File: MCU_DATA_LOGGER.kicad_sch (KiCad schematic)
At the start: 0 parts

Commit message: Have added symbols
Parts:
- added BT?: Battery, symbol Device:Battery
- added C? (x4): C, symbol Device:C
- added C?: C_Polarized, symbol Device:C_Polarized
- added D? (x3): LED, symbol Device:LED
- added H? (x4): MountingHole, symbol Mechanical:MountingHole
- added R? (x7): R, symbol Device:R
- added U? (x2): 24LC1025, symbol Memory_EEPROM:24LC1025
- added U?: ATMEGA328P-AU, QFP80P900X900X120-32N, symbol ATMEGA328P-AU:ATMEGA328P-AU
- added U?: DS1337S+, SOIC127P600X175-8N, symbol New_Library:DS1337S+
- added Y? (x2): Crystal, symbol Device:Crystal
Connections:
- new net: D?.1 (K), D?.1 (K)
- new net: D?.2 (A), D?.2 (A)
- new net: U?.21 (GND), U?.3 (GND), U?.5 (GND)
- new net: U?.4 (VCC), U?.6 (VCC)
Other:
- added sheet Connectors (connectors.kicad_sch)

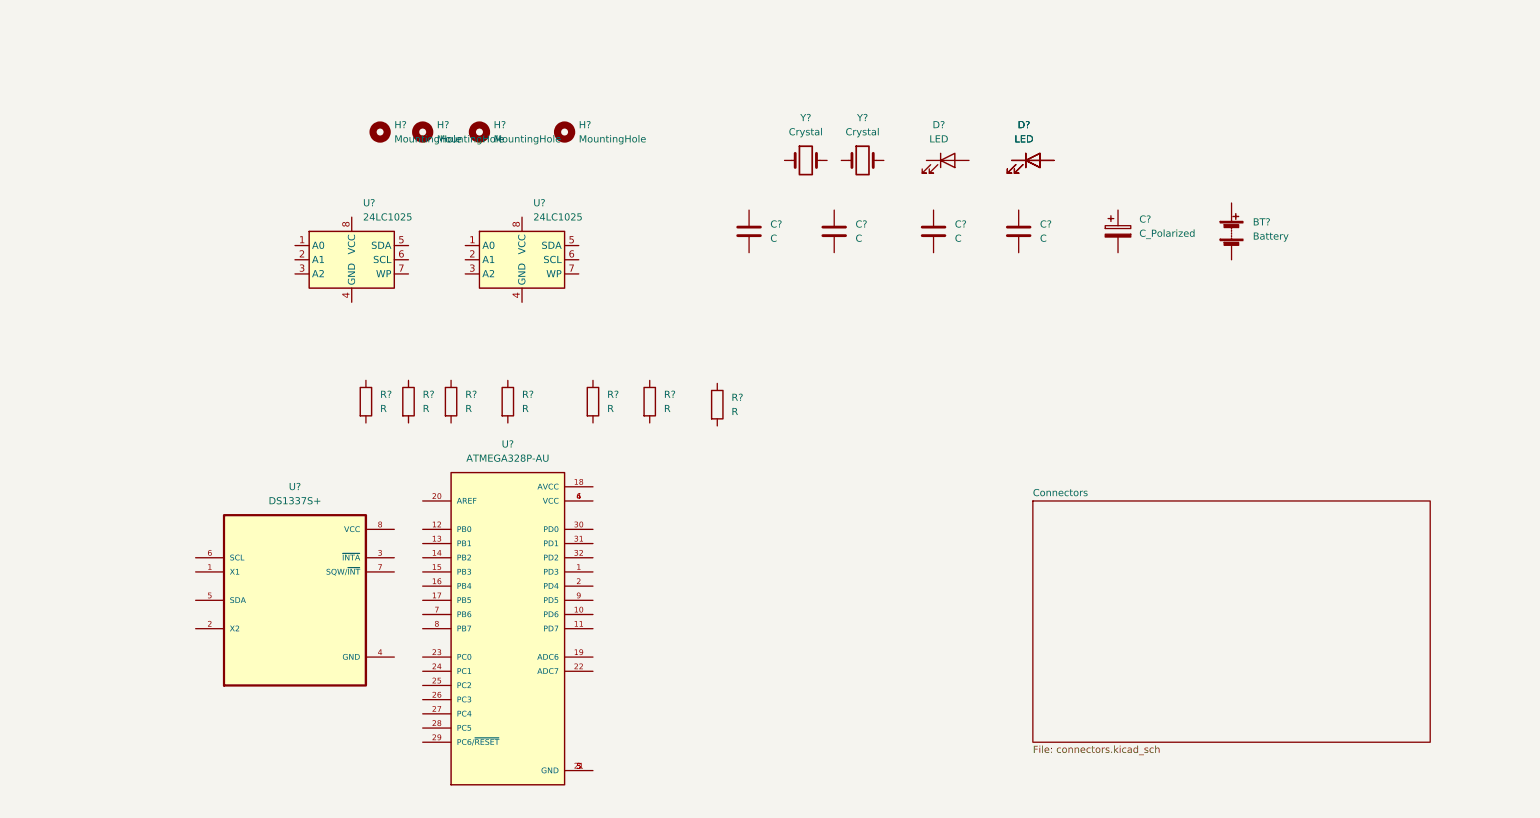
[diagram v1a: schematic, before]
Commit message: Added components values
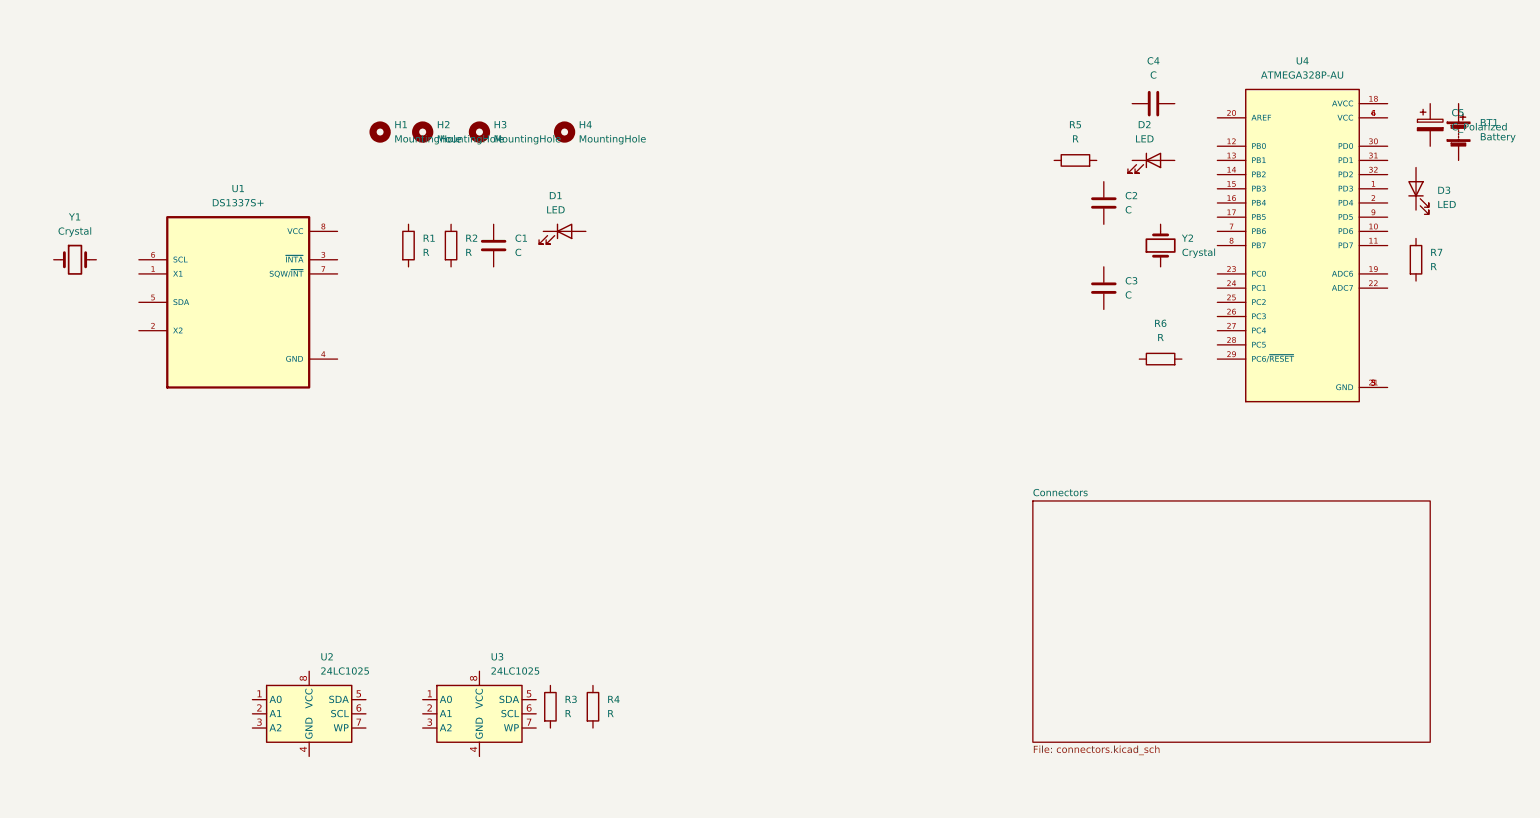
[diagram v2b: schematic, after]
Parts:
- gave numbers to parts that had none: 26
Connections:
- net at D3.1 (K): no longer D2.1 (K)
- net at D3.2 (A): no longer D2.2 (A)
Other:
- moved on the sheet: BT1, C1, C2, C3, C4, C5, D1, D2, D3, R1, R2, R3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

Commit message: Completed symbol footpring associations
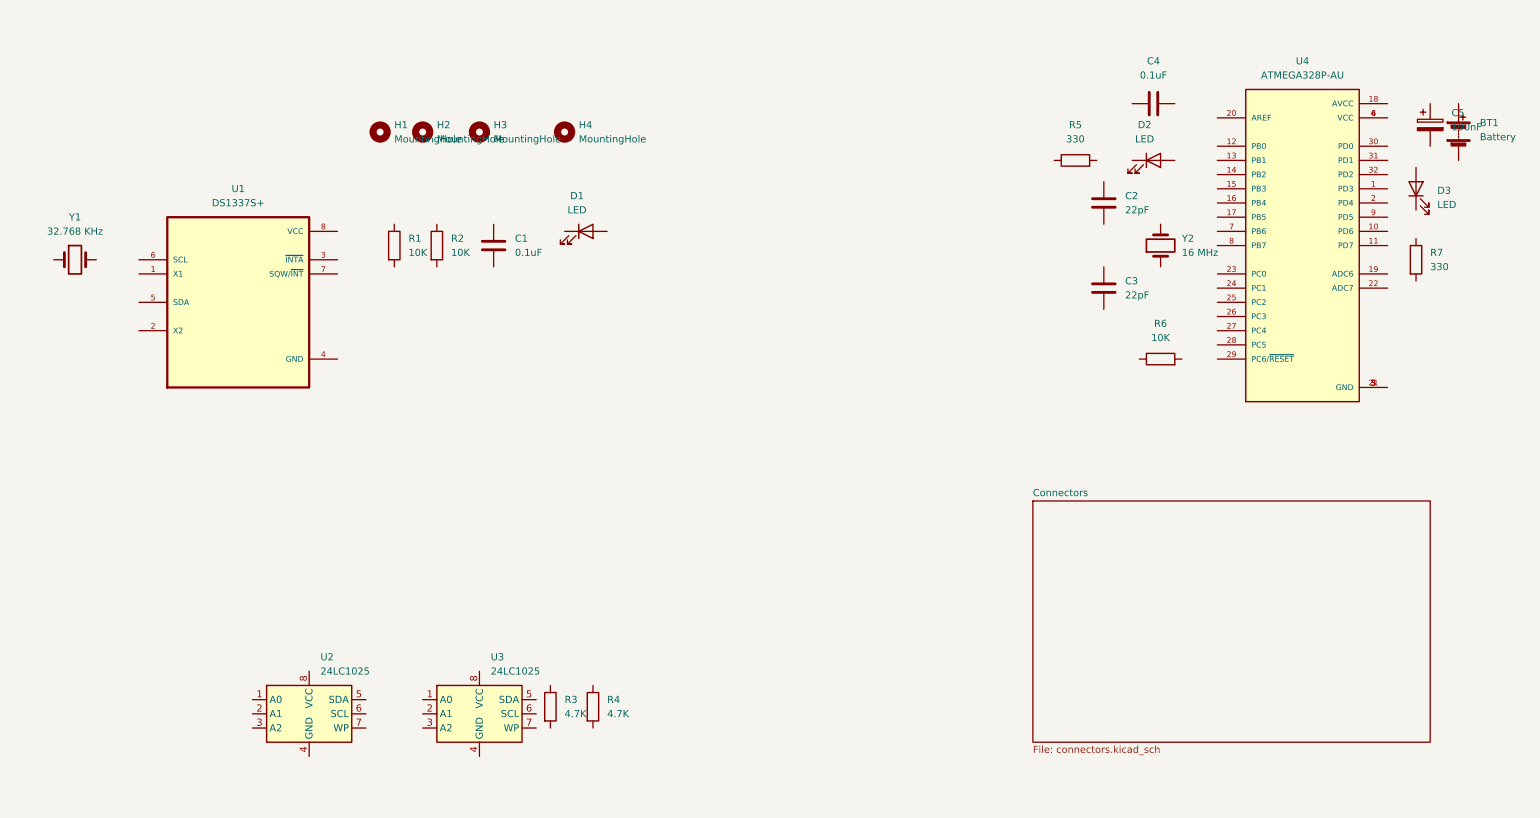
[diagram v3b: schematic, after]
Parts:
- BT1: footprint (none) -> DS1337S_:SOIC127P600X175-8N
- C1, C4: value C -> 0.1uF; footprint (none) -> Capacitor_SMD:C_0805_2012Metric
- C2, C3: value C -> 22pF; footprint (none) -> Capacitor_SMD:C_0805_2012Metric
- C5: value C_Polarized -> 100nF; footprint (none) -> Capacitor_SMD:C_0805_2012Metric
- D1, D2, D3: footprint (none) -> LED_SMD:LED_0805_2012Metric
- H1, H2, H3, H4: footprint (none) -> MountingHole:MountingHole_2.1mm
- R1, R2, R6: value R -> 10K; footprint (none) -> Resistor_SMD:R_0805_2012Metric
- R3, R4: value R -> 4.7K; footprint (none) -> Resistor_SMD:R_0805_2012Metric
- R5, R7: value R -> 330; footprint (none) -> Resistor_SMD:R_0805_2012Metric
- U1: footprint SOIC127P600X175-8N -> DS1337S_:SOIC127P600X175-8N
- U2, U3: footprint (none) -> Package_SO:SOIC-8_5.23x5.23mm_P1.27mm
- U4: footprint QFP80P900X900X120-32N -> ATMEGA:QFP80P900X900X120-32N
- Y1: value Crystal -> 32.768 KHz; footprint (none) -> Crystal:Crystal_SMD_5032-2Pin_5.0x3.2mm_HandSoldering
- Y2: value Crystal -> 16 MHz; footprint (none) -> Crystal:Crystal_SMD_5032-2Pin_5.0x3.2mm_HandSoldering
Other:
- moved on the sheet: D1, R1, R2

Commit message: completed wiring of main sheet
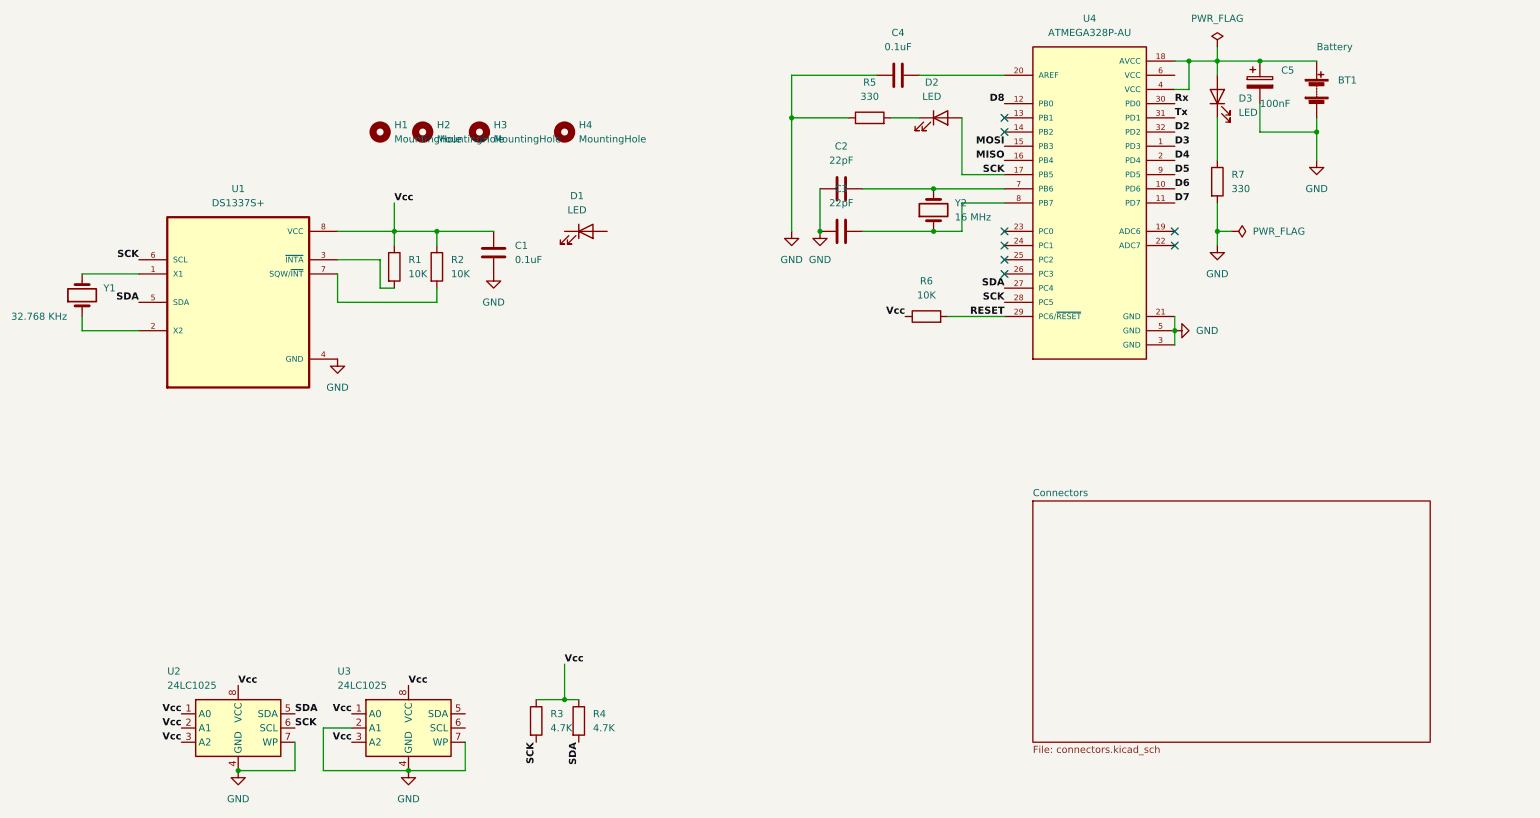
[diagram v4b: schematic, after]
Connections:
- net GND: now reaches C4.1
- net GND: now also BT1.2 (-), C1.2, C2.1, C3.1, C5.2, R5.1, R7.2, U1.4 (GND), U2.4 (GND), U2.7 (WP), U3.2 (A1), U3.4 (GND), U3.7 (WP), U4.21 (GND), U4.3 (GND), U4.5 (GND)
- net at C4.2: now also U4.20 (AREF)
- net at Y1.1: now also U1.2 (X2)
- net at Y1.2: now also U1.1 (X1)
- net Vcc: now reaches U2.1 (A0)
- net Vcc: now also C1.1, R1.1, R2.1, R3.1, R4.1, R6.1, U1.8 (VCC), U2.2 (A1), U2.3 (A2), U2.8 (VCC), U3.1 (A0), U3.3 (A2), U3.8 (VCC)
- net SDA: now reaches U2.5 (SDA)
- net SDA: now also R4.2, U1.5 (SDA), U4.27 (PC4)
- net SCK: now reaches U2.6 (SCL)
- net SCK: now also D2.2 (A), R3.2, U1.6 (SCL), U4.17 (PB5), U4.28 (PC5)
- net at C3.2: now also U4.8 (PB7), Y2.1
- net at R5.2: now also D2.1 (K)
- net at C2.2: now also U4.7 (PB6), Y2.2
- net at R1.2: now also U1.3 (~{INTA})
- net at R7.1: now also D3.1 (K)
- net at D3.2 (A): now also BT1.1 (+), C5.1, U4.18 (AVCC), U4.4 (VCC)
- net RESET: now reaches R6.2
- net RESET: now also U4.29 (PC6/~{RESET})
- net at R2.2: now also U1.7 (SQW/~{INT})
- net D3: now reaches U4.1 (PD3)
- net D6: now reaches U4.10 (PD6)
- net D7: now reaches U4.11 (PD7)
- net D8: now reaches U4.12 (PB0)
- net MOSI: now reaches U4.15 (PB3)
- net MISO: now reaches U4.16 (PB4)
- net D4: now reaches U4.2 (PD4)
- net Rx: now reaches U4.30 (PD0)
- net Tx: now reaches U4.31 (PD1)
- net D2: now reaches U4.32 (PD2)
- net at U4.6 (VCC): no longer U4.4 (VCC)
- net D5: now reaches U4.9 (PD5)
- no-connect marks 0 -> 8
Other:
- moved on the sheet: BT1, C1, C2, C3, C4, C5, D2, D3, R1, R2, R3, R4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

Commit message: Completed wiring in all sheets
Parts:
- removed D1: LED, LED_SMD:LED_0805_2012Metric, symbol Device:LED
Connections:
- net SCK: now also U3.6 (SCL)
- net SDA: now also U3.5 (SDA)
- no-connect marks 8 -> 9
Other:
- sheet Connectors ports: added D2, D3, D4, D5, D6, D7, D8, GND, MISO, MOSI, RESET, Rx, SCK, SDA, Tx, Vcc; removed none

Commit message: Completed schematic
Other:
- note added: "EEPROM (MEMORY)"
- note added: "MCU"
- note added: "MOUNTING"
- note added: "REAL TIME CLOCK"
- moved on the sheet: BT1, C1, C2, C3, C4, C5, D2, D3, H1, H2, H3, H4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

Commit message: Completed placement of footprints
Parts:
- BT1: footprint DS1337S_:SOIC127P600X175-8N -> Connector_PinHeader_2.54mm:PinHeader_1x02_P2.54mm_Vertical
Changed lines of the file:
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@@
       (effects (font (size 1.27 1.27)) (justify left))
     )
-    (property "Footprint" "DS1337S_:SOIC127P600X175-8N" (id 2) (at 251.46 46.736 90)
+    (property "Footprint" "Connector_PinHeader_2.54mm:PinHeader_1x02_P2.54mm_Vertical" (id 2) (at 251.46 46.736 90)
       (effects (font (size 1.27 1.27)) hide)
     )
@@
     )
     (path "/c4cbdec2-7bd4-4cee-8ad0-c4c5f2090f87"
-      (reference "BT1") (unit 1) (value "Battery") (footprint "DS1337S_:SOIC127P600X175-8N")
+      (reference "BT1") (unit 1) (value "Battery") (footprint "Connector_PinHeader_2.54mm:PinHeader_1x02_P2.54mm_Vertical")
     )
     (path "/af6b8cdb-2e7f-4ff9-bb75-06e45d8b39d4"

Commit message: Routing GND Vcc completed
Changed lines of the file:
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@@
     (effects (font (size 1.27 1.27) bold) (justify left bottom))
   )
-  (label "Tx" (at 223.52 132.08 180)
+  (label "Rx" (at 223.52 132.08 180)
     (effects (font (size 1.27 1.27) bold) (justify right bottom))
   )
